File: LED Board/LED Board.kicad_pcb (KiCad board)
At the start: 2 copper layers, 47 x 10 mm, 8 parts, among them U1 gnd_spring, U2 gnd_conn, U3 power_conn, U4 power_conn, U5 gnd_conn, U6 gnd_spring

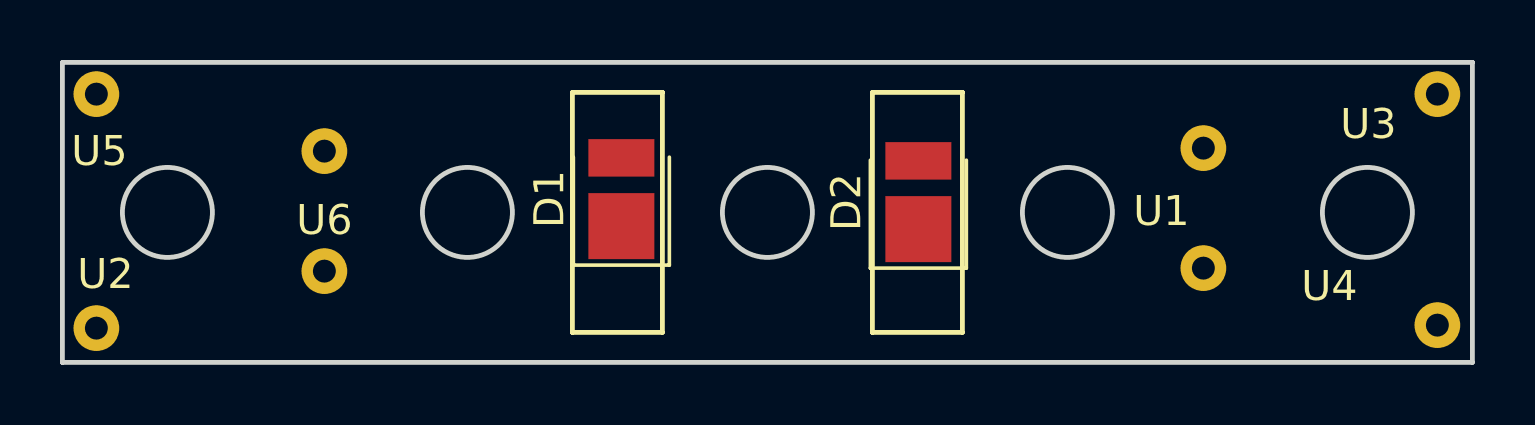
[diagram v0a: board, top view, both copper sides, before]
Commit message: led fix error
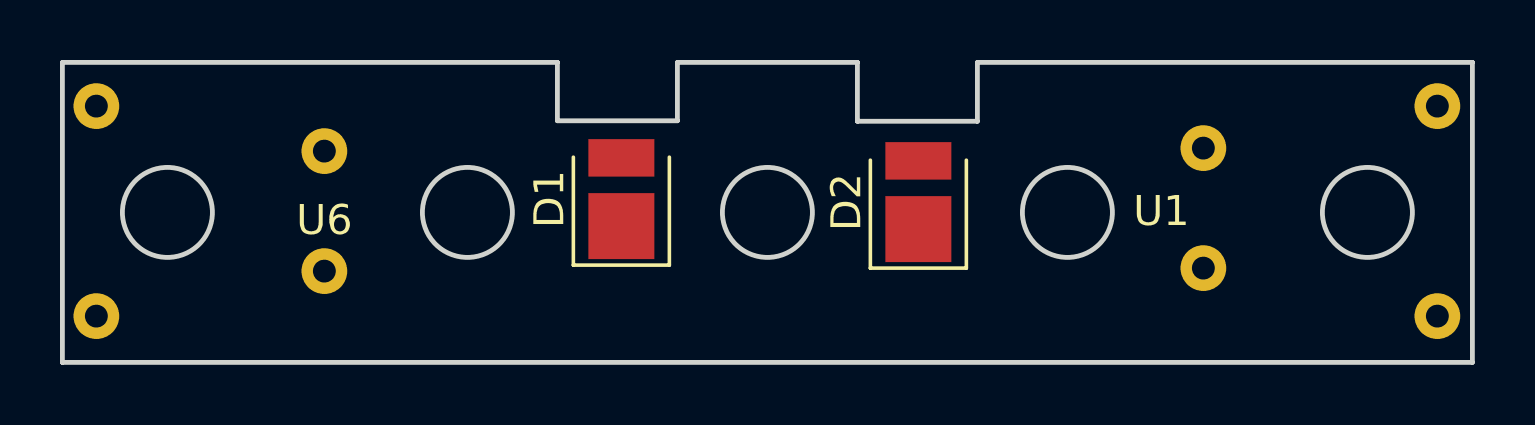
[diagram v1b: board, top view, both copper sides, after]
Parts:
- U2, U3, U4, U5: moved to B.Cu
- moved U2 0.40 mm to (84.1, 109.0)
- moved U3 0.40 mm to (128.8, 102.0)
- moved U5 0.40 mm to (84.1, 102.0)
- moved U4 0.30 mm to (128.8, 109.0)
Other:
- outline, holes or cut-outs redrawn
